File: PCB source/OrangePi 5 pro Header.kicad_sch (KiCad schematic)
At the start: 7 parts, among them J2 Orange pi 5 pro

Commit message: Do Cleanup
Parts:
- renumbered C23 to C1, C35 to C2, C36 to C3, C37 to C4, C38 to C5, C39 to C6
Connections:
- net FAN_PWM: now also J2.6 (GPIO1_A7/PWM3)
- net ON OFF BTN: now also J2.26 (GPIO1_A4)
- net STATUS LED: now also J2.11 (GPIO1_B0)
- net USER BUTTON: now also J2.25 (GPIO1_A6)
- net USER LED 1: now also J2.24 (GPIO1_D7/I2C8_SDA/PWM15)
- net USER LED 2: now also J2.23 (GPIO4_A7/I2C5_SDA)
- no-connect marks 26 -> 20

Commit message: Pass ERC
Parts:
- added R40: 20kΩ, PCM_JLCPCB:R_0402, symbol PCM_JLCPCB-Resistors:0402,20kΩ
- added R41: 10kΩ, PCM_JLCPCB:R_0402, symbol PCM_JLCPCB-Resistors:0402,10kΩ
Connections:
- net GND: now also R41.2
- net at J2.22 (GPIO4_A6/UART3_RX/I2C5_SCL): now also R40.2, R41.1
- new net BUCK_EN: R40.1
- no-connect marks 20 -> 19

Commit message: Prepare board for layout
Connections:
- net USB_OUT.+ renamed USB_OUT.D+
- net USB_OUT.- renamed USB_OUT.D-
- net USB_SBC.+ renamed USB_SBC.D+
- net USB_SBC.- renamed USB_SBC.D-
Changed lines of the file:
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@@
+	)
+	(bus_entry
+		(at 190.5 63.5)
+		(size -2.54 -2.54)
+		(stroke
+			(width 0)
+			(type default)
+		)
+	)
+	(bus_entry
+		(at 53.34 68.58)
+		(size 2.54 -2.54)
+		(stroke
+			(width 0)
+			(type default)
+		)
 	)
 	(bus_entry
@@
 	)
 	(bus_entry
-		(at 190.5 63.5)
-		(size -2.54 -2.54)
-		(stroke
-			(width 0)
-			(type default)
-		)
-	)
-	(bus_entry
-		(at 53.34 68.58)
-		(size 2.54 -2.54)
-		(stroke
-			(width 0)
-			(type default)
-		)
-	)
-	(bus_entry
-		(at 242.57 132.08)
-		(size -2.54 -2.54)
-		(stroke
-			(width 0)
-			(type default)
-		)
-	)
-	(bus_entry
 		(at 53.34 72.39)
 		(size 2.54 -2.54)
+		(stroke
+			(width 0)
+			(type default)
+		)
+	)
+	(bus_entry
+		(at 242.57 133.35)
+		(size -2.54 -2.54)
 		(stroke
 			(width 0)
@@
 	(wire
 		(pts
-			(xy 105.41 156.21) (xy 118.11 156.21)
-		)
-		(stroke
-			(width 0)
-			(type default)
-		)
-	)
-	(bus
-		(pts
-			(xy 242.57 129.54) (xy 242.57 132.08)
+			(xy 93.98 156.21) (xy 118.11 156.21)
 		)
 		(stroke
@@
 		)
 	)
-	(wire
-		(pts
-			(xy 196.85 127) (xy 207.01 127)
-		)
-		(stroke
-			(width 0)
-			(type default)
-		)
-	)
-	(bus
-		(pts
-			(xy 242.57 132.08) (xy 242.57 135.89)
+	(bus
+		(pts
+			(xy 209.55 132.08) (xy 209.55 135.89)
+		)
+		(stroke
+			(width 0)
+			(type default)
+		)
+	)
+	(bus
+		(pts
+			(xy 242.57 129.54) (xy 242.57 133.35)
 		)
 		(stroke
@@
 		)
 	)
-	(bus
-		(pts
-			(xy 209.55 132.08) (xy 209.55 135.89)
-		)
-		(stroke
-			(width 0)
-			(type default)
-		)
-	)
 	(wire
 		(pts
@@
 		)
 	)
+	(wire
+		(pts
+			(xy 227.33 130.81) (xy 240.03 130.81)
+		)
+		(stroke
+			(width 0)
+			(type default)
+		)
+	)
+	(bus
+		(pts
+			(xy 242.57 133.35) (xy 242.57 135.89)
+		)
+		(stroke
+			(width 0)
+			(type default)
+		)
+	)
 	(bus
 		(pts
@@
 	(wire
 		(pts
-			(xy 105.41 152.4) (xy 114.3 152.4)
+			(xy 93.98 152.4) (xy 114.3 152.4)
 		)
 		(stroke
@@
 	(wire
 		(pts
+			(xy 227.33 127) (xy 240.03 127)
+		)
+		(stroke
+			(width 0)
+			(type default)
+		)
+	)
+	(wire
+		(pts
 			(xy 175.26 130.81) (xy 175.26 128.27)
 		)
@@
 	(wire
 		(pts
+			(xy 191.77 129.54) (xy 207.01 129.54)
+		)
+		(stroke
+			(width 0)
+			(type default)
+		)
+	)
+	(wire
+		(pts
 			(xy 172.72 116.84) (xy 175.26 116.84)
 		)
@@
 	(wire
 		(pts
-			(xy 207.01 129.54) (xy 196.85 129.54)
-		)
-		(stroke
-			(width 0)
-			(type default)
-		)
-	)
-	(wire
-		(pts
 			(xy 175.26 116.84) (xy 175.26 113.03)
 		)
@@
 	(wire
 		(pts
+			(xy 191.77 127) (xy 207.01 127)
+		)
+		(stroke
+			(width 0)
+			(type default)
+		)
+	)
+	(wire
+		(pts
 			(xy 256.54 64.77) (xy 256.54 59.69)
 		)
@@
 	(wire
 		(pts
-			(xy 228.6 129.54) (xy 240.03 129.54)
-		)
-		(stroke
-			(width 0)
-			(type default)
-		)
-	)
-	(wire
-		(pts
 			(xy 92.71 44.45) (xy 95.25 44.45)
 		)
@@
 	(wire
 		(pts
-			(xy 228.6 127) (xy 240.03 127)
-		)
-		(stroke
-			(width 0)
-			(type default)
-		)
-	)
-	(wire
-		(pts
 			(xy 175.26 113.03) (xy 172.72 113.03)
 		)
@@
 		)
 	)
-	(label "CAN_TR.TXD"
-		(at 62.23 69.85 0)
+	(label "USB_OUT.D-"
+		(at 227.33 130.81 0)
 		(fields_autoplaced yes)
 		(effects
@@
 		)
 	)
-	(label "USB_OUT.+"
-		(at 105.41 156.21 180)
-		(fields_autoplaced yes)
-		(effects
-			(font
-				(size 1.27 1.27)
-			)
-			(justify right bottom)
-		)
-	)
-	(label "USB_OUT.-"
-		(at 228.6 129.54 0)
+	(label "CAN_TR.TXD"
+		(at 62.23 69.85 0)
 		(fields_autoplaced yes)
 		(effects
@@
 		)
 	)
-	(label "USB_SBC.+"
-		(at 196.85 127 0)
+	(label "USB_OUT.D+"
+		(at 93.98 156.21 0)
 		(fields_autoplaced yes)
 		(effects
@@
 		)
 	)
-	(label "CAN_TR.RXD"
-		(at 62.23 66.04 0)
+	(label "USB_SBC.D+"
+		(at 191.77 127 0)
 		(fields_autoplaced yes)
 		(effects
@@
 		)
 	)
-	(label "USB_OUT.+"
-		(at 228.6 127 0)
+	(label "CAN_TR.RXD"
+		(at 62.23 66.04 0)
 		(fields_autoplaced yes)
 		(effects
@@
 		)
 	)
-	(label "USB_SBC.-"
-		(at 196.85 129.54 0)
+	(label "USB_SBC.D-"
+		(at 143.51 157.48 0)
 		(fields_autoplaced yes)
 		(effects
@@
 		)
 	)
-	(label "USB_OUT.-"
-		(at 105.41 152.4 180)
-		(fields_autoplaced yes)
-		(effects
-			(font
-				(size 1.27 1.27)
-			)
-			(justify right bottom)
-		)
-	)
-	(label "UART_DEBUG.TX"
-		(at 172.72 57.15 0)
+	(label "USB_OUT.D-"
+		(at 93.98 152.4 0)
 		(fields_autoplaced yes)
 		(effects
@@
 		)
 	)
-	(label "UART_DEBUG.RX"
-		(at 172.72 60.96 0)
+	(label "USB_OUT.D+"
+		(at 227.33 127 0)
 		(fields_autoplaced yes)
 		(effects
@@
 		)
 	)
-	(label "USB_SBC.+"
+	(label "USB_SBC.D+"
 		(at 143.51 153.67 0)
 		(fields_autoplaced yes)
@@
 		)
 	)
-	(label "USB_SBC.-"
-		(at 143.51 157.48 0)
-		(fields_autoplaced yes)
-		(effects
+	(label "UART_DEBUG.TX"
+		(at 172.72 57.15 0)
+		(fields_autoplaced yes)
+		(effects
+			(font
+				(size 1.27 1.27)
+			)
+			(justify left bottom)
+		)
+	)
+	(label "UART_DEBUG.RX"
+		(at 172.72 60.96 0)
+		(fields_autoplaced yes)
+		(effects
+			(font
+				(size 1.27 1.27)
+			)
+			(justify left bottom)
+		)
+	)
+	(label "USB_SBC.D-"
+		(at 191.77 129.54 0)
+		(fields_autoplaced yes)
+		(effects

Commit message: Do buck Layout
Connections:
- net +3V3: no longer names the net of J2.32 (3V3)
- net +3V3: no longer J2.40 (3V3)
- no-connect marks 19 -> 21
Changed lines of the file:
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@@
-	)
-	(junction
-		(at 92.71 44.45)
-		(diameter 0)
-		(color 0 0 0 0)
 	)
 	(junction
@@
 	)
 	(no_connect
+		(at 95.25 44.45)
+	)
+	(no_connect
 		(at 172.72 83.82)
 	)
@@
 	(no_connect
 		(at 172.72 102.87)
+	)
+	(no_connect
+		(at 95.25 46.99)
 	)
 	(no_connect
@@
 	(wire
 		(pts
-			(xy 92.71 46.99) (xy 92.71 44.45)
-		)
-		(stroke
-			(width 0)
-			(type default)
-		)
-	)
-	(wire
-		(pts
 			(xy 222.25 64.77) (xy 210.82 64.77)
 		)
@@
 		)
 	)
-	(wire
-		(pts
-			(xy 95.25 46.99) (xy 92.71 46.99)
-		)
-		(stroke
-			(width 0)
-			(type default)
-		)
-	)
 	(bus
 		(pts
@@
 	(wire
 		(pts
-			(xy 92.71 43.18) (xy 92.71 44.45)
-		)
-		(stroke
-			(width 0)
-			(type default)
-		)
-	)
-	(wire
-		(pts
 			(xy 175.26 45.72) (xy 175.26 48.26)
 		)
@@
 		(pts
 			(xy 172.72 120.65) (xy 175.26 120.65)
-		)
-		(stroke
-			(width 0)
-			(type default)
-		)
-	)
-	(wire
-		(pts
-			(xy 92.71 44.45) (xy 95.25 44.45)
 		)
 		(stroke
@@
 					(unit 1)
 				)
-			)
-		)
-	)
-	(symbol
-		(lib_id "power:+3V3")
-		(at 92.71 43.18 0)
-		(unit 1)
-		(exclude_from_sim no)
-		(in_bom yes)
-		(on_board yes)
-		(dnp no)
-		(fields_autoplaced yes)
-		(property "Reference" "#PWR025"
-			(at 92.71 46.99 0)
-			(effects
-				(font
-					(size 1.27 1.27)
-				)
-				(hide yes)
-			)
-		)
-		(property "Value" "+3V3"
-			(at 92.71 38.1 0)
-			(effects
-				(font
-					(size 1.27 1.27)
-				)
-			)
-		)
-		(property "Footprint" ""
-			(at 92.71 43.18 0)
-			(effects
-				(font
-					(size 1.27 1.27)
-				)
-				(hide yes)
-			)
-		)
-		(property "Datasheet" ""
-			(at 92.71 43.18 0)
-			(effects
-				(font
-					(size 1.27 1.27)
-				)
-				(hide yes)
-			)
-		)
-		(property "Description" "Power symbol creates a global label with name \"+3V3\""
-			(at 92.71 43.18 0)
-			(effects
-				(font
-					(size 1.27 1.27)
-				)
-				(hide yes)
-			)
-		)
-		(pin "1"
-		)
-		(instances
-			(project "OrangePie"
-				(path "/3103c9de-f1ba-4d51-8bfc-798df1c75e2f/d2960c43-83cc-4db9-89f3-db63fa692eb6"
-					(reference "#PWR025")
-					(unit 1)
-				)

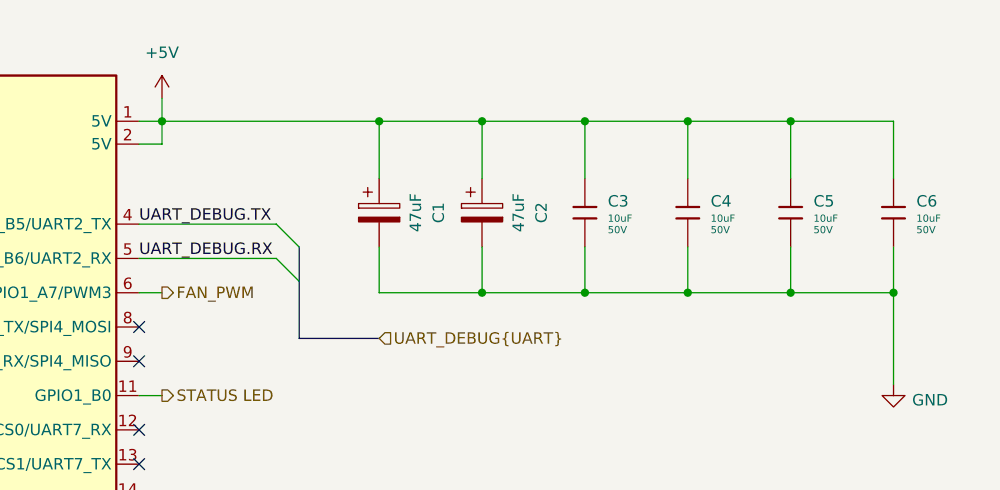
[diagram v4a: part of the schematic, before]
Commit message: Create v1 floorplan
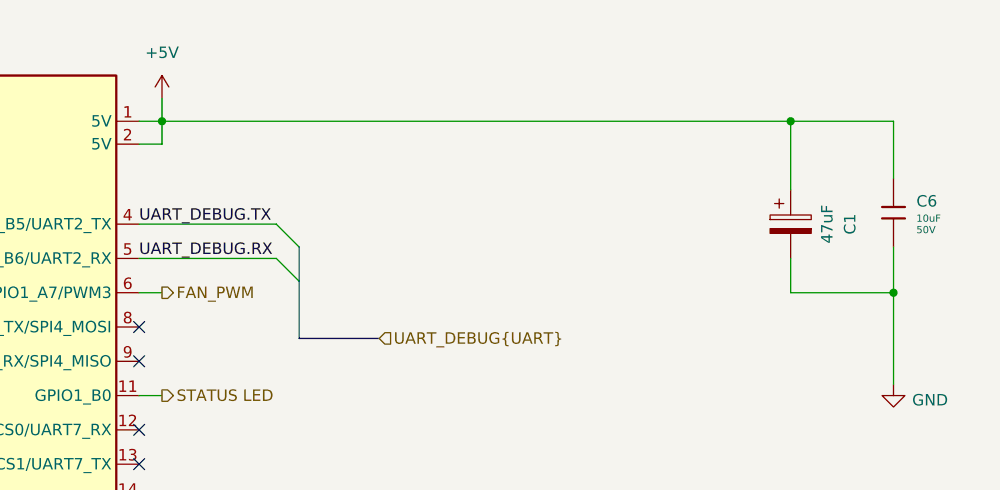
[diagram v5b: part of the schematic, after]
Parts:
- removed C2: 47uF, Capacitor_SMD:CP_Elec_6.3x5.4, symbol Device:C_Polarized
- removed C3, C4, C5: 10uF, PCM_JLCPCB:C_1206, symbol PCM_JLCPCB-Capacitors:1206,10uF
- C1: footprint Capacitor_SMD:CP_Elec_6.3x5.4 -> Capacitor_SMD:CP_Elec_4x5.4
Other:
- moved on the sheet: C1

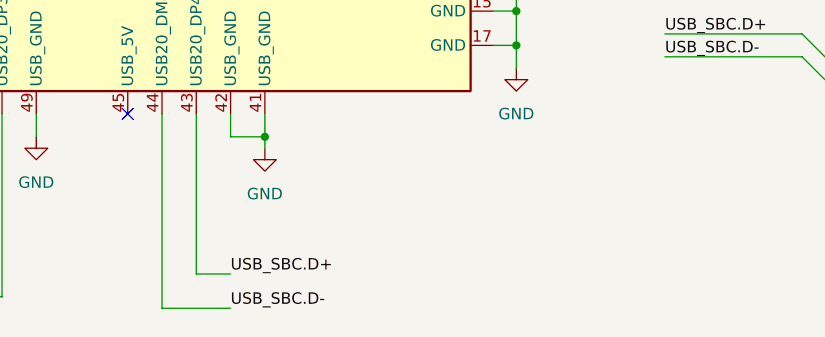
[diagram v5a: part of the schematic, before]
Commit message: Add 22R resistors to USB
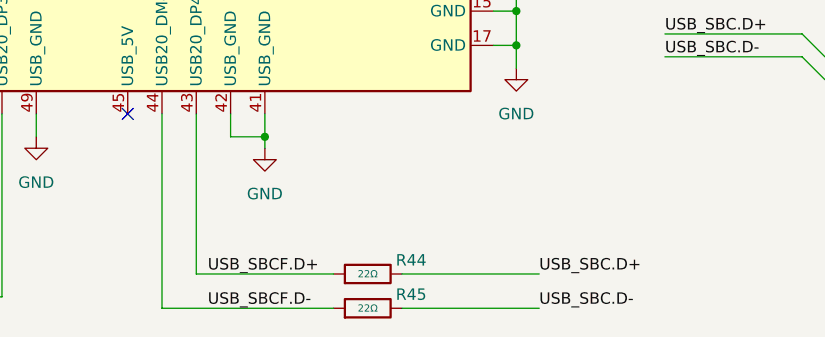
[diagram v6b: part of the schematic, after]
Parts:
- added R44, R45: 22Ω, PCM_JLCPCB:R_0402, symbol PCM_JLCPCB-Resistors:0402,22Ω
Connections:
- net USB_SBC.D+: now also R44.2; no longer J2.43 (USB20_DP4)
- net USB_SBC.D-: now also R45.2; no longer J2.44 (USB20_DM4)
- new net USB_SBCF.D+: J2.43 (USB20_DP4), R44.1
- new net USB_SBCF.D-: J2.44 (USB20_DM4), R45.1

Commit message: Fix schematic
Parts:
- removed C1: 47uF, Capacitor_SMD:CP_Elec_4x5.4, symbol Device:C_Polarized
- added C1: 47uF 50V RVT1H470M0607, Capacitor_SMD:CP_Elec_6.3x7.7, symbol Device:C_Polarized_Small
- C6: Price 0.031USD -> 0.035USD; Stock 4852625 -> 821695
- R40: Stock 1747699 -> 1163119
- R41: Stock 6666349 -> 13746052
- R44, R45: Stock 2497993 -> 2158519
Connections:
- net +5V: now also C1.1
- net GND: now also C1.2
- net DAC RST: now reaches J2.14 (GPIO1_A3/I2C4_SCL/PWM1/SPI4_CS0)
- net CAN RST: now reaches J2.27 (GPIO1_A2/SPI4_CLK/PWM0/I2C4_SDA)
- no-connect marks 21 -> 19
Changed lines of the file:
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@@
 (kicad_sch
-	(version 20231120)
+	(version 20250114)
 	(generator "eeschema")
-	(generator_version "8.0")
+	(generator_version "9.0")
 	(paper "A4")
 	(title_block
@@
 	)
 	(no_connect
-		(at 172.72 87.63)
-	)
-	(no_connect
 		(at 172.72 99.06)
 	)
@@
 	(no_connect
 		(at 95.25 46.99)
-	)
-	(no_connect
-		(at 95.25 88.9)
 	)
 	(bus_entry
@@
 	(wire
 		(pts
-			(xy 245.11 60.96) (xy 245.11 64.77)
+			(xy 245.11 58.42) (xy 245.11 64.77)
 		)
 		(stroke
@@
 	(wire
 		(pts
+			(xy 83.82 88.9) (xy 95.25 88.9)
+		)
+		(stroke
+			(width 0)
+			(type default)
+		)
+	)
+	(wire
+		(pts
 			(xy 172.72 116.84) (xy 175.26 116.84)
 		)
@@
 	(wire
 		(pts
+			(xy 172.72 87.63) (xy 175.26 87.63)
+		)
+		(stroke
+			(width 0)
+			(type default)
+		)
+	)
+	(wire
+		(pts
 			(xy 83.82 100.33) (xy 95.25 100.33)
 		)
@@
 	(wire
 		(pts
-			(xy 245.11 53.34) (xy 245.11 45.72)
-		)
-		(stroke
-			(width 0)
-			(type default)
-		)
-	)
-	(wire
-		(pts
 			(xy 91.44 123.19) (xy 95.25 123.19)
 		)
@@
 		(pts
 			(xy 59.69 107.95) (xy 95.25 107.95)
+		)
+		(stroke
+			(width 0)
+			(type default)
+		)
+	)
+	(wire
+		(pts
+			(xy 245.11 45.72) (xy 245.11 53.34)
 		)
 		(stroke
@@
 	(label "USB_SBCF.D-"
 		(at 140.97 157.48 0)
-		(fields_autoplaced yes)
 		(effects
 			(font
@@
 	(label "USB_OUT.D-"
 		(at 227.33 130.81 0)
-		(fields_autoplaced yes)
 		(effects
 			(font
@@
 	(label "CAN_TR.TXD"
 		(at 62.23 69.85 0)
-		(fields_autoplaced yes)
 		(effects
 			(font
@@
 	(label "USB_OUT.D+"
 		(at 93.98 156.21 0)
-		(fields_autoplaced yes)
 		(effects
 			(font
@@
 	(label "USB_SBC.D+"
 		(at 191.77 127 0)
-		(fields_autoplaced yes)
 		(effects
 			(font
@@
 	(label "CAN_TR.RXD"
 		(at 62.23 66.04 0)
-		(fields_autoplaced yes)
 		(effects
 			(font
@@
 	(label "USB_SBC.D-"
 		(at 177.8 157.48 0)
-		(fields_autoplaced yes)
 		(effects
 			(font
@@
 	(label "USB_OUT.D-"
 		(at 93.98 152.4 0)
-		(fields_autoplaced yes)
 		(effects
 			(font
@@
 	(label "USB_SBCF.D+"
 		(at 140.97 153.67 0)
-		(fields_autoplaced yes)
 		(effects
 			(font
@@
 	(label "USB_OUT.D+"
 		(at 227.33 127 0)
-		(fields_autoplaced yes)
 		(effects
 			(font
@@
 	(label "USB_SBC.D+"
 		(at 177.8 153.67 0)
-		(fields_autoplaced yes)
 		(effects
 			(font
@@
 	(label "UART_DEBUG.TX"
 		(at 172.72 57.15 0)
-		(fields_autoplaced yes)
 		(effects
 			(font
@@
 	(label "UART_DEBUG.RX"
 		(at 172.72 60.96 0)
-		(fields_autoplaced yes)
 		(effects
 			(font
@@
 	(label "USB_SBC.D-"
 		(at 191.77 129.54 0)
-		(fields_autoplaced yes)
 		(effects
 			(font
@@
 		(shape output)
 		(at 175.26 76.2 0)
-		(fields_autoplaced yes)
 		(effects
 			(font
@@
 		(shape output)
 		(at 175.26 64.77 0)
-		(fields_autoplaced yes)
 		(effects
 			(font
@@
 		(shape output)
 		(at 83.82 100.33 180)
-		(fields_autoplaced yes)
 		(effects
 			(font
@@
 		(shape input)
 		(at 50.8 96.52 180)
-		(fields_autoplaced yes)
 		(effects
 			(font
@@
 		(shape input)
 		(at 83.82 92.71 180)
-		(fields_autoplaced yes)
 		(effects
 			(font
@@
 			)
 			(justify right)
+		)
+	)
+	(hierarchical_label "DAC RST"
+		(shape input)
+		(at 175.26 87.63 0)
+		(effects
+			(font
+				(size 1.27 1.27)
+			)
+			(justify left)
 		)
 	)
@@
 		(shape input)
 		(at 212.09 135.89 0)
-		(fields_autoplaced yes)
 		(effects
 			(font
@@
 		(shape output)
 		(at 83.82 104.14 180)
-		(fields_autoplaced yes)
 		(effects
 			(font
@@
 		(shape input)
 		(at 199.39 69.85 0)
-		(fields_autoplaced yes)
 		(effects
 			(font
@@
 		(shape input)
 		(at 83.82 96.52 180)
-		(fields_autoplaced yes)
+		(effects
+			(font
+				(size 1.27 1.27)
+			)
+			(justify right)
+		)
+	)
+	(hierarchical_label "CAN RST"
+		(shape input)
+		(at 83.82 88.9 180)
 		(effects
 			(font
@@
 		(shape input)
 		(at 45.72 74.93 180)
-		(fields_autoplaced yes)
 		(effects
 			(font
@@
 		(shape input)
 		(at 248.92 135.89 0)
-		(fields_autoplaced yes)
 		(effects
 			(font
@@
 	)
 	(symbol
+		(lib_id "Device:C_Polarized_Small")
+		(at 245.11 55.88 0)
+		(unit 1)
+		(exclude_from_sim no)
+		(in_bom yes)
+		(on_board yes)
+		(dnp no)
+		(property "Reference" "C1"
+			(at 240.538 56.388 0)
+			(effects
+				(font
+					(size 1.27 1.27)
+				)
+			)
+		)
+		(property "Value" "47uF 50V RVT1H470M0607"
+			(at 229.87 58.674 0)
+			(effects
+				(font
+					(size 1.27 1.27)
+				)
+			)
+		)
+		(property "Footprint" "Capacitor_SMD:CP_Elec_6.3x7.7"
+			(at 245.11 55.88 0)
+			(effects
+				(font
+					(size 1.27 1.27)
+				)
+				(hide yes)
+			)
+		)
+		(property "Datasheet" "~"
+			(at 245.11 55.88 0)
+			(effects
+				(font
+					(size 1.27 1.27)
+				)
+				(hide yes)
+			)
+		)
+		(property "Description" "Polarized capacitor, small symbol"
+			(at 245.11 55.88 0)
+			(effects
+				(font
+					(size 1.27 1.27)
+				)
+				(hide yes)
+			)
+		)
+		(pin "1"
+		)
+		(pin "2"
+		)
+		(instances
+			(project "OrangePie"
+				(path "/3103c9de-f1ba-4d51-8bfc-798df1c75e2f/d2960c43-83cc-4db9-89f3-db63fa692eb6"
+					(reference "C1")
+					(unit 1)
+				)
+			)
+		)
+	)
+	(symbol
 		(lib_id "PCM_JLCPCB-Resistors:0402,22Ω")
 		(at 158.75 153.67 90)
@@
 			)
 		)
-		(property "Stock" "2497993"
+		(property "Stock" "2158519"
 			(at 158.75 153.67 0)
 			(effects
@@
 			)
 		)
-		(property "Stock" "1747699"
+		(property "Stock" "1163119"
 			(at 59.69 102.87 0)
 			(effects
@@
 				(path "/3103c9de-f1ba-4d51-8bfc-798df1c75e2f/d2960c43-83cc-4db9-89f3-db63fa692eb6"
 					(reference "R40")
-					(unit 1)
-				)
-			)
-		)
-	)
-	(symbol
-		(lib_id "Device:C_Polarized")
-		(at 245.11 57.15 0)
-		(unit 1)
-		(exclude_from_sim no)
-		(in_bom yes)
-		(on_board yes)
-		(dnp no)
-		(property "Reference" "C1"
-			(at 251.714 57.15 90)
-			(effects
-				(font
-					(size 1.27 1.27)
-				)
-			)
-		)
-		(property "Value" "47uF"
-			(at 249.174 57.15 90)
-			(effects
-				(font
-					(size 1.27 1.27)
-				)
-			)
-		)
-		(property "Footprint" "Capacitor_SMD:CP_Elec_4x5.4"
-			(at 246.0752 60.96 0)
-			(effects
-				(font
-					(size 1.27 1.27)
-				)
-				(hide yes)
-			)
-		)
-		(property "Datasheet" "~"
-			(at 245.11 57.15 0)
-			(effects
-				(font
-					(size 1.27 1.27)
-				)
-				(hide yes)
-			)
-		)
-		(property "Description" "Polarized capacitor"
-			(at 245.11 57.15 0)
-			(effects
-				(font
-					(size 1.27 1.27)
-				)
-				(hide yes)
-			)
-		)
-		(property "LCSC" " C90276"
-			(at 245.11 57.15 90)
-			(effects
-				(font
-					(size 1.27 1.27)
-				)
-				(hide yes)
-			)
-		)
-		(property "MPN" "VT1V470M0605"
-			(at 245.11 57.15 90)
-			(effects
-				(font
-					(size 1.27 1.27)
-				)
-				(hide yes)
-			)
-		)
-		(pin "1"
-		)
-		(pin "2"
-		)
-		(instances
-			(project "OrangePie"
-				(path "/3103c9de-f1ba-4d51-8bfc-798df1c75e2f/d2960c43-83cc-4db9-89f3-db63fa692eb6"
-					(reference "C1")
 					(unit 1)
 				)
@@
 			)
 		)
-		(property "Stock" "6666349"
+		(property "Stock" "13746052"
 			(at 59.69 113.03 0)
 			(effects
@@
 			)
 		)
-		(property "Stock" "4852625"
+		(property "Stock" "821695"
 			(at 256.54 55.88 0)
 			(effects
@@
 			)
 		)
-		(property "Price" "0.031USD"
+		(property "Price" "0.035USD"
 			(at 256.54 55.88 0)
 			(effects
@@
 			)
 		)
-		(property "Stock" "2497993"
+		(property "Stock" "2158519"
 			(at 158.75 157.48 0)
 			(effects

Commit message: production ready
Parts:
- removed C1: 47uF 50V RVT1H470M0607, Capacitor_SMD:CP_Elec_6.3x7.7, symbol Device:C_Polarized_Small
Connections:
- net CAN_3V3_ON: now reaches J2.9 (GPIO1_A0/UART6_RX/SPI4_MISO)
- no-connect marks 19 -> 18
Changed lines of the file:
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@@
-	)
-	(junction
-		(at 256.54 64.77)
-		(diameter 0)
-		(color 0 0 0 0)
-	)
-	(junction
-		(at 245.11 45.72)
-		(diameter 0)
-		(color 0 0 0 0)
 	)
 	(junction
@@
 	)
 	(no_connect
-		(at 172.72 72.39)
-	)
-	(no_connect
 		(at 172.72 102.87)
 	)
@@
 	(wire
 		(pts
-			(xy 245.11 58.42) (xy 245.11 64.77)
-		)
-		(stroke
-			(width 0)
-			(type default)
-		)
-	)
-	(wire
-		(pts
 			(xy 227.33 130.81) (xy 240.03 130.81)
 		)
@@
 	(wire
 		(pts
-			(xy 245.11 64.77) (xy 256.54 64.77)
-		)
-		(stroke
-			(width 0)
-			(type default)
-		)
-	)
-	(wire
-		(pts
 			(xy 172.72 45.72) (xy 175.26 45.72)
 		)
@@
 	(wire
 		(pts
-			(xy 175.26 45.72) (xy 245.11 45.72)
+			(xy 175.26 45.72) (xy 256.54 45.72)
 		)
 		(stroke
@@
 	(wire
 		(pts
-			(xy 256.54 64.77) (xy 256.54 59.69)
+			(xy 256.54 59.69) (xy 256.54 74.93)
 		)
 		(stroke
@@
 	(wire
 		(pts
-			(xy 256.54 74.93) (xy 256.54 64.77)
-		)
-		(stroke
-			(width 0)
-			(type default)
-		)
-	)
-	(wire
-		(pts
 			(xy 172.72 120.65) (xy 175.26 120.65)
 		)
@@
 	(wire
 		(pts
-			(xy 245.11 45.72) (xy 256.54 45.72)
+			(xy 172.72 72.39) (xy 175.26 72.39)
 		)
 		(stroke
@@
 		(pts
 			(xy 59.69 107.95) (xy 95.25 107.95)
-		)
-		(stroke
-			(width 0)
-			(type default)
-		)
-	)
-	(wire
-		(pts
-			(xy 245.11 45.72) (xy 245.11 53.34)
 		)
 		(stroke
@@
 			)
 			(justify right)
+		)
+	)
+	(hierarchical_label "CAN_3V3_ON"
+		(shape output)
+		(at 175.26 72.39 0)
+		(effects
+			(font
+				(size 1.27 1.27)
+			)
+			(justify left)
 		)
 	)
@@
 					(unit 1)
 				)
-			)
-		)
-	)
-	(symbol
-		(lib_id "Device:C_Polarized_Small")
-		(at 245.11 55.88 0)
-		(unit 1)
-		(exclude_from_sim no)
-		(in_bom yes)
-		(on_board yes)
-		(dnp no)
-		(property "Reference" "C1"
-			(at 240.538 56.388 0)
-			(effects
-				(font
-					(size 1.27 1.27)
-				)
-			)
-		)
-		(property "Value" "47uF 50V RVT1H470M0607"
-			(at 229.87 58.674 0)
-			(effects
-				(font
-					(size 1.27 1.27)
-				)
-			)
-		)
-		(property "Footprint" "Capacitor_SMD:CP_Elec_6.3x7.7"
-			(at 245.11 55.88 0)
-			(effects
-				(font
-					(size 1.27 1.27)
-				)
-				(hide yes)
-			)
-		)
-		(property "Datasheet" "~"
-			(at 245.11 55.88 0)
-			(effects
-				(font
-					(size 1.27 1.27)
-				)
-				(hide yes)
-			)
-		)
-		(property "Description" "Polarized capacitor, small symbol"
-			(at 245.11 55.88 0)
-			(effects
-				(font
-					(size 1.27 1.27)
-				)
-				(hide yes)
-			)
-		)
-		(pin "1"
-		)
-		(pin "2"
-		)
-		(instances
-			(project "OrangePie"
-				(path "/3103c9de-f1ba-4d51-8bfc-798df1c75e2f/d2960c43-83cc-4db9-89f3-db63fa692eb6"
-					(reference "C1")
-					(unit 1)
-				)
